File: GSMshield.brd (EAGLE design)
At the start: 68.6 x 53.3 mm, 65 parts, among them IC1 RT8289, IC2 SIM900, J1 SIM Socket, J2 Antenna, J3 Breakout 1, J4 Breakout 2, J5 ARDUINO-SHIELD_R3, Q1 2N7002, Q2 2N7002, Q3 2N7002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

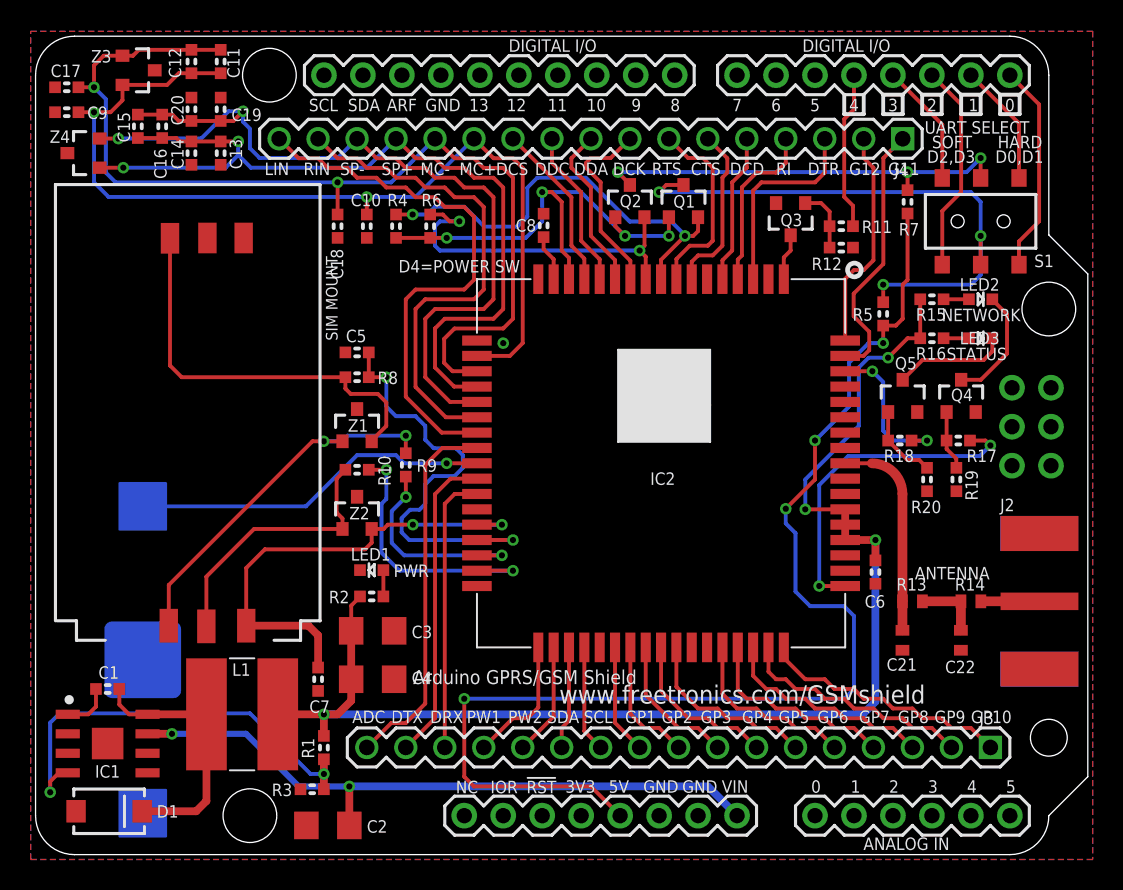
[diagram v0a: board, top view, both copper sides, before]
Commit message: Changed all fonts to vector Increased VIA size Added version number and license to overlay Added chip orientation markers in tdocu layer Repositioned designators
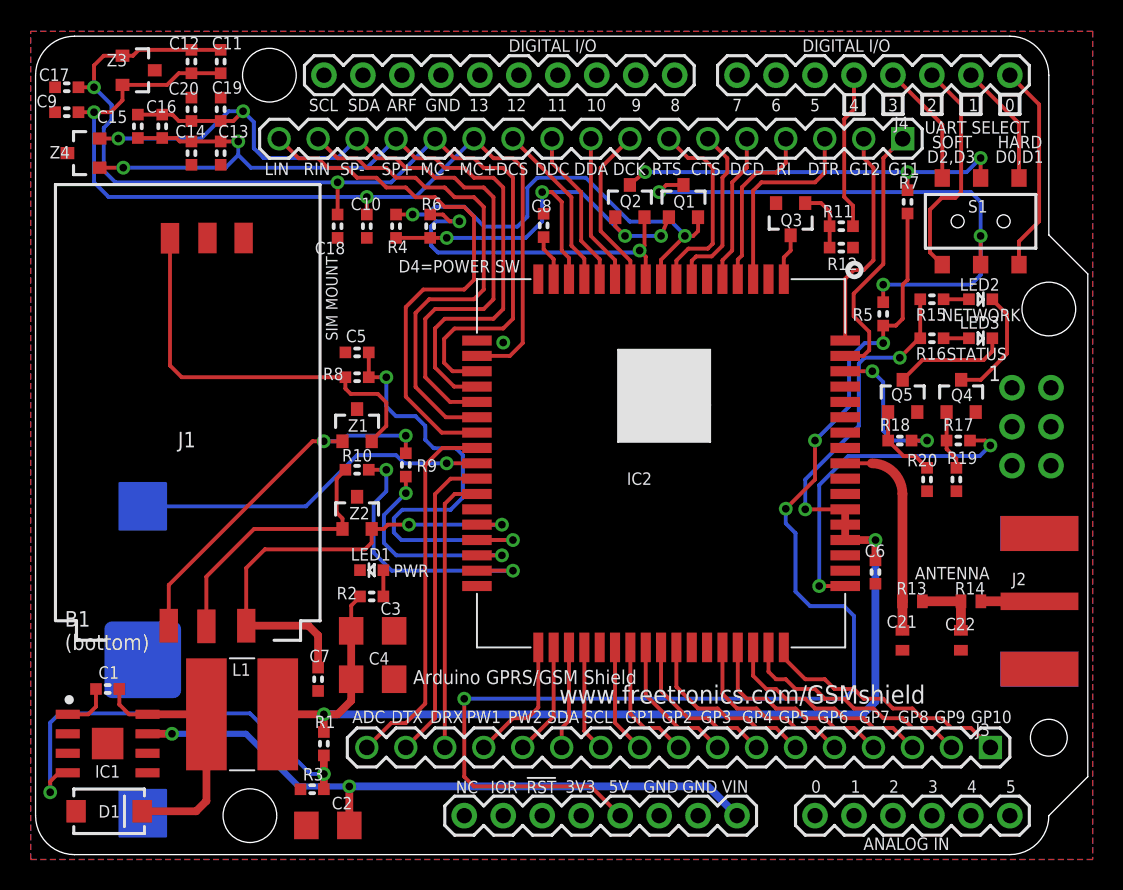
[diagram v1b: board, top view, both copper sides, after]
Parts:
- C2: value 10µF -> 10uF
- C21, C22: value NP -> NOT PLACED
- C3, C4: value 47µF -> 47uF
- L1: value 10µH -> 10uH
- R1: value 27 kΩ -> 27K
- R10, R8, R9: value 22Ω -> 22R
- R11, R17, R18: value 10Ω -> 10R
- R12, R19, R20: value 100kΩ -> 100K
- R13, R14: value 0Ω -> 0R
- R15, R16, R2: value 1kΩ -> 1K
- R3: value 12 kΩ -> 12K
- R4, R5, R6, R7: value 10kΩ -> 10K
- moved R1 0.25 mm to (19.4, 7.86)
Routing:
- net RXD_5V: track 27.7 -> 26.0 mm
- net DISP_CLK: track 12.3 -> 10.7 mm
- net SIM_DATA: track 29.1 -> 30.6 mm
- net D2: track 13.6 -> 14.8 mm
- net DISP_DATA: track 10.9 -> 9.80 mm
- net SIM_CLK: track 13.9 -> 14.6 mm
- net SIM_RST: track 18.1 -> 18.8 mm
- net RXD: track 22.9 -> 23.5 mm
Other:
- board text added: "1"
- board text added: "A"
- board text added: "B1 (bottom)"
- board text added: "Copyright 2013 Freetronics Pty Ltd Released under the terms of the TAPR Open Hardware License www.tapr.org/ohl"
- board text added: "GSM/GPRS Shield for Arduino"
- board text added: "J1"
- board text added: "K"
- board text added: "v1.0 SKU: GSM"
- board text added: "www.freetronics.com/gsm"
- board text removed: "Arduino GSM/GPRS Shield"
